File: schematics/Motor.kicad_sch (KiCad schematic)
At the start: 29 parts, among them U4 STM32G031F8Px, X2 8MHz

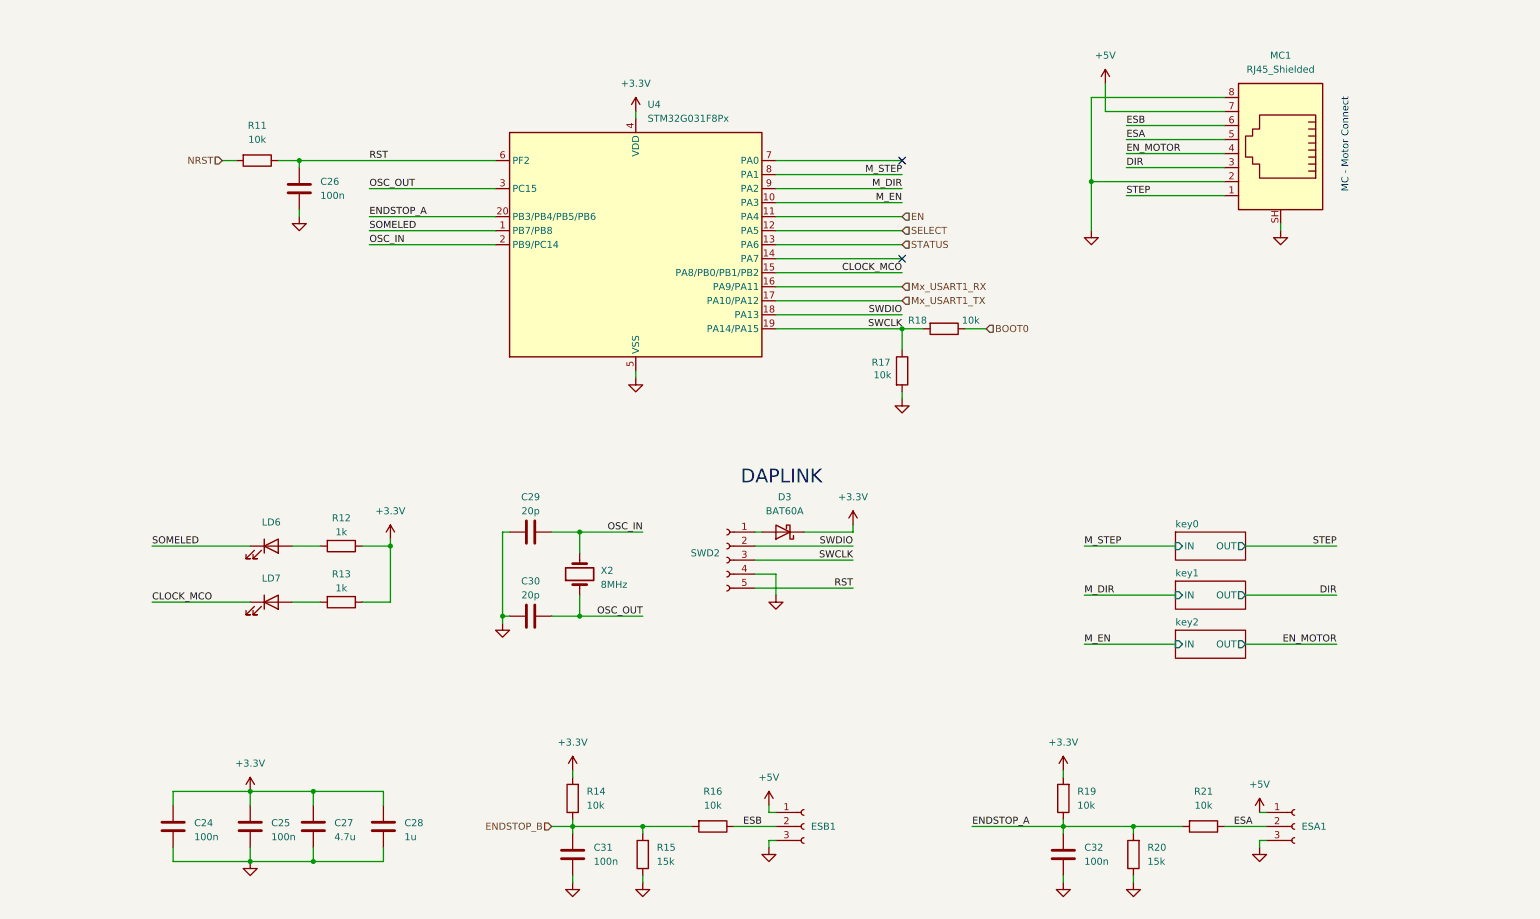
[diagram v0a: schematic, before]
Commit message: Обновил схемотехнику у платы. Убрал лишнее компоненты и лишнии линии
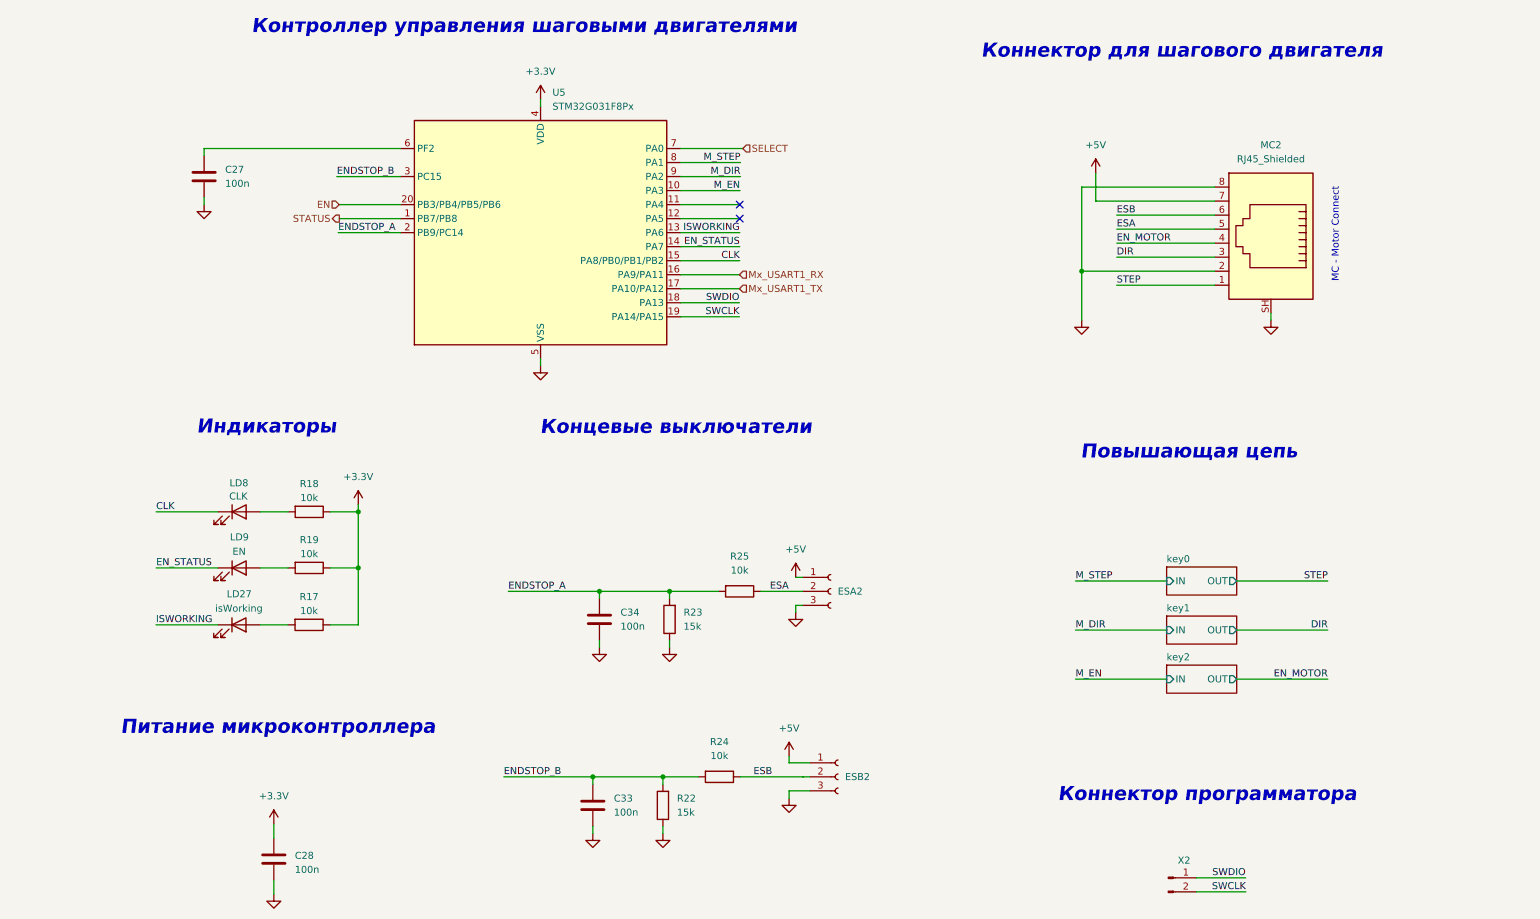
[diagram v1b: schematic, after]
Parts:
- removed C24: 100n, Capacitor_SMD:C_0805_2012Metric, symbol Device:C
- removed C27: 4.7u, Capacitor_SMD:C_0805_2012Metric, symbol Device:C
- removed C28: 1u, Capacitor_SMD:C_0805_2012Metric, symbol Device:C
- removed C29, C30: 20p, Capacitor_SMD:C_0805_2012Metric, symbol Device:C
- removed D3: BAT60A, Diode_SMD:D_SOD-323, symbol Diode:BAT60A
- removed R11, R14, R18, R19: 10k, Resistor_SMD:R_0805_2012Metric, symbol Device:R
- removed SWD2: Conn_01x05_Socket, Connector_PinSocket_2.54mm:PinSocket_1x05_P2.54mm_Vertical, symbol Connector:Conn_01x05_Socket
- removed X2: 8MHz, Crystal:Crystal_HC49-U_Vertical, symbol Device:Crystal
- added LD27: isWorking, LED_SMD:LED_0805_2012Metric, symbol Device:LED
- added X2: Conn_01x02_Pin, Connector_PinHeader_2.54mm:PinHeader_1x02_P2.54mm_Vertical, symbol Connector:Conn_01x02_Pin
- LD8: renamed from LD6; value ~ -> CLK
- LD9: renamed from LD7; value ~ -> EN
- R18: renamed from R12; value 1k -> 10k
- R19: renamed from R13; value 1k -> 10k
- renumbered C26 to C27, C25 to C28, C31 to C33, C32 to C34, ESA1 to ESA2, ESB1 to ESB2, MC1 to MC2, R15 to R22, R20 to R23, R16 to R24, R21 to R25, U4 to U5
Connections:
- net OSC_IN is gone; now on net ENDSTOP_A: U5.2 (PB9/PC14)
- net OSC_OUT is gone; now on net ENDSTOP_B: U5.3 (PC15)
- net +3.3V: now also R17.1
- net EN: now also U5.20 (PB3/PB4/PB5/PB6); no longer U5.11 (PA4)
- net ENDSTOP_A: no longer U5.20 (PB3/PB4/PB5/PB6)
- net GND: no longer R17.2
- net SELECT: now also U5.7 (PA0); no longer U5.12 (PA5)
- net STATUS: now also U5.1 (PB7/PB8); no longer U5.13 (PA6)
- net SWCLK: now also X2.2 (Pin_2); no longer R17.1
- net SWDIO: now also X2.1 (Pin_1)
- net EN_STATUS: now reaches U5.14 (PA7)
- net EN_STATUS: now also LD9.1 (K)
- net CLOCK_MCO renamed CLK
- net CLK: now also LD8.1 (K); no longer LD9.1 (K)
- net RST: no longer names the net of C27.1, U5.6 (PF2)
- removed net SOMELED: LD8.1 (K), U5.1 (PB7/PB8)
- new net: LD27.2 (A), R17.2
- new net ISWORKING: LD27.1 (K), U5.13 (PA6)
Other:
- note added: "Индикаторы"
- note added: "Коннектор для шагового двигателя"
- note added: "Коннектор программатора"
- note added: "Контроллер управления шаговыми двигателями"
- note added: "Концевые выключатели"
- note added: "Питание микроконтроллера"
- note added: "Повышающая цепь"
- note removed: "DAPLINK"
- company: (none) -> МГТУ им. Н.Э.Баумана
- moved on the sheet: C27, C28, C33, C34, ESA2, ESB2, LD8, LD9, MC2, R18, R19, R22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

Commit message: Обновлена нумерация элементов
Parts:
- renumbered C27 to C21, C28 to C22, C33 to C23, C34 to C24, ESA2 to ESA1, ESB2 to ESB1, LD27 to LD6, LD8 to LD7, LD9 to LD8, MC2 to MC1, R17 to R13, R18 to R14, R19 to R15, R22 to R16, R23 to R17, R24 to R18, R25 to R19, U5 to U4, X2 to X1

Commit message: Переименновал разъемы
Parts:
- renumbered ESA1 to ESA2, ESB1 to ESB2, MC1 to MC2
